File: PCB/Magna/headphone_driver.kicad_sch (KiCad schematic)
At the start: 0 parts

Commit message: Update analogue frontend and add potentiometer interface
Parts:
- added C1201, C1204: 100n, symbol Device:C
- added C1202, C1203, C1205, C1206, C1207, C1208: 100u, symbol Device:C_Polarized
- added C1209, C1210: 22uF, symbol Device:C_Polarized
- added C1211, C1212: 100pF, symbol Device:C
- added C1213, C1214: 220uF, symbol Device:C_Polarized
- added J1201: AudioJack3, symbol Connector_Audio:AudioJack3
- added R1201, R1202: 4R7, symbol Device:R
- added R1203, R1204: 10k, symbol Device:R
- added R1205, R1206, R1211, R1212: 22k, symbol Device:R
- added R1207, R1208: 680R, symbol Device:R
- added R1209, R1210: 1k3, symbol Device:R
- added R1213, R1214: 100R, symbol Device:R
- added RV1201: 10k, symbol Device:R_Potentiometer_Dual_Separate
- added U1201, U1202: NE5532, symbol Amplifier_Operational:NE5532
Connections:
- new net: C1212.2, C1214.1, R1210.2, RV1201.4, U1202.7
- new net: C1210.1, RV1201.5
- new net: C1208.2, RV1201.6
- new net: C1202.2, C1204.1, J1201.R
- new net: C1201.1, C1203.2, J1201.T
- new net: C1209.2, R1205.1, U1201.3 (+)
- new net: R1207.1, U1201.1, U1201.2 (-)
- new net: C1211.2, C1213.1, R1209.2, RV1201.1, U1201.7
- new net: C1213.2, R1211.1, R1213.1
- new net: R1208.1, U1202.1, U1202.2 (-)
- new net: C1212.1, R1208.2, R1210.1, U1202.6 (-)
- new net: C1209.1, RV1201.2
- new net: C1207.2, RV1201.3
- new net: C1214.2, R1212.1, R1214.1
- new net: R1204.1, R1214.2
- new net: R1203.1, R1213.2
- new net: C1210.2, R1206.1, U1202.3 (+)
- new net: C1211.1, R1207.2, R1209.1, U1201.6 (-)
- new net: C1204.2, R1202.1
- new net: C1201.2, R1201.1
- new net AudioInL: C1207.1
- new net AudioInR: C1208.1
- new net GND: J1201.S, R1201.2, R1202.2
- new net VAA_BIAS_L: C1205.2, R1203.2, R1205.2, R1211.2, U1201.5 (+)
- new net VAA_BIAS_R: C1206.2, R1204.2, R1206.2, R1212.2, U1202.5 (+)
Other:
- note added: "TDA2822D"

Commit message: Add final touched to all schematics
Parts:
- added C1215, C1216: 100nF/16V, Capacitor_SMD:C_0402_1005Metric, symbol Device:C
- added unit 3 of U1201
- added unit 3 of U1202
- renumbered C1207 to C1201, C1208 to C1202, C1209 to C1203, C1210 to C1204, C1211 to C1205, C1212 to C1206, C1213 to C1207, C1214 to C1208, C1205 to C1209, C1206 to C1210, C1203 to C1211, C1202 to C1212, C1201 to C1213, C1204 to C1214, R1205 to R1201, R1206 to R1202, R1207 to R1203, R1208 to R1204, R1209 to R1205, R1210 to R1206, R1211 to R1207, R1212 to R1208, R1213 to R1209, R1214 to R1210, R1203 to R1211, R1204 to R1212, R1201 to R1213, R1202 to R1214
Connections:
- net GND: now also C1215.2, C1216.2, U1201.4 (V-), U1202.4 (V-)
- new net VAA: C1215.1, C1216.1, U1201.8 (V+), U1202.8 (V+)

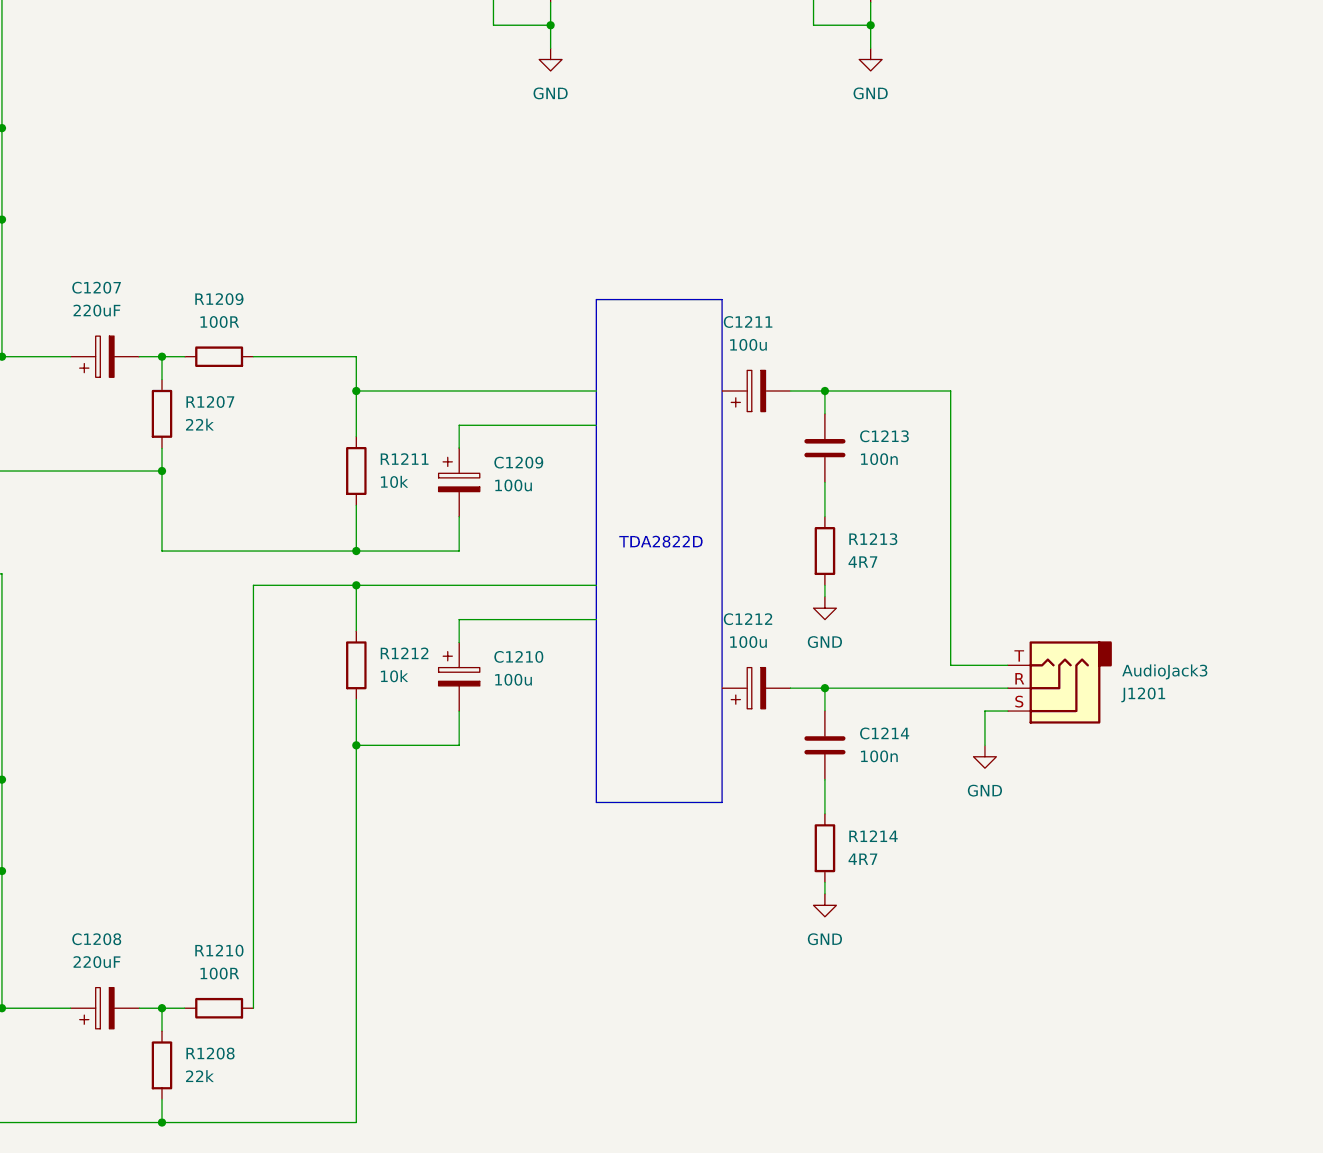
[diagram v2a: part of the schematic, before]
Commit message: Remove all ERC in schematics
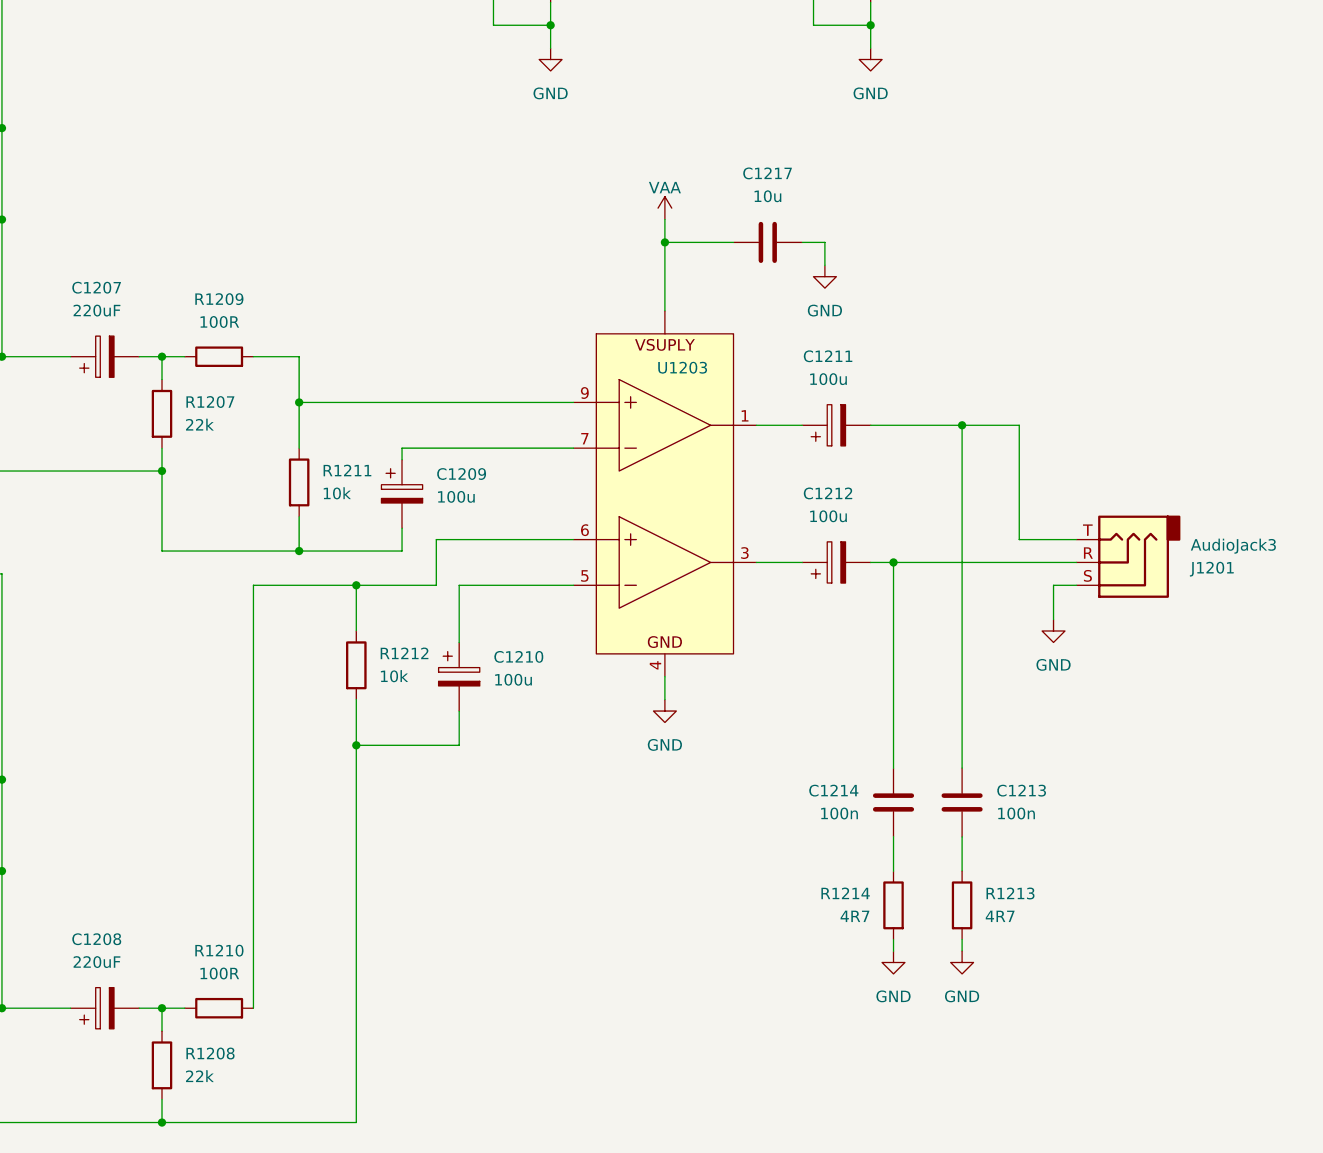
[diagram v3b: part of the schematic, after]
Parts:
- added C1217: 10u, symbol Device:C
- added U1203: ~, symbol Skrooter_symbols:TDA2822D
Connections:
- net GND: now also C1217.2, U1203.4 (GND)
- net VAA: now also C1217.1, U1203. (VCC)
- net at C1210.1: now also U1203.5 (Input2+)
- net at C1209.1: now also U1203.7 (Input1+)
- net at R1210.2, R1212.1: now also U1203.6 (Input2-)
- net at R1209.2, R1211.1: now also U1203.9 (Input1-)
- net at C1212.1: now also U1203.3 (OUTPUT2)
- net at C1211.1: now also U1203.1 (OUTPUT1)
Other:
- note removed: "TDA2822D"
- moved on the sheet: C1209, C1211, C1212, C1213, C1214, J1201, R1211, R1213, R1214

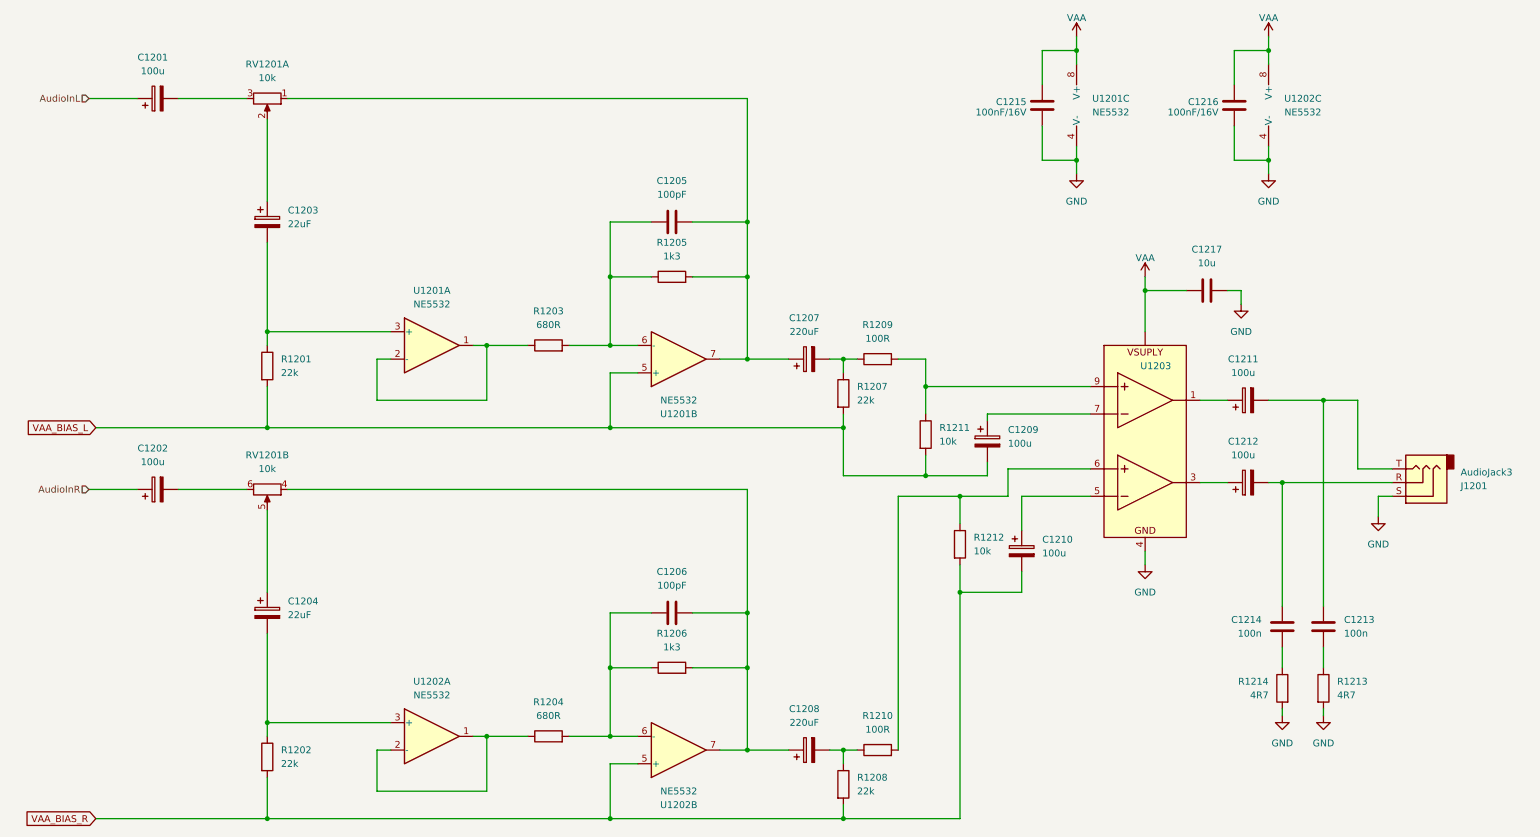
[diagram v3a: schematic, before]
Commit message: Update capacitors to parts in JLC library
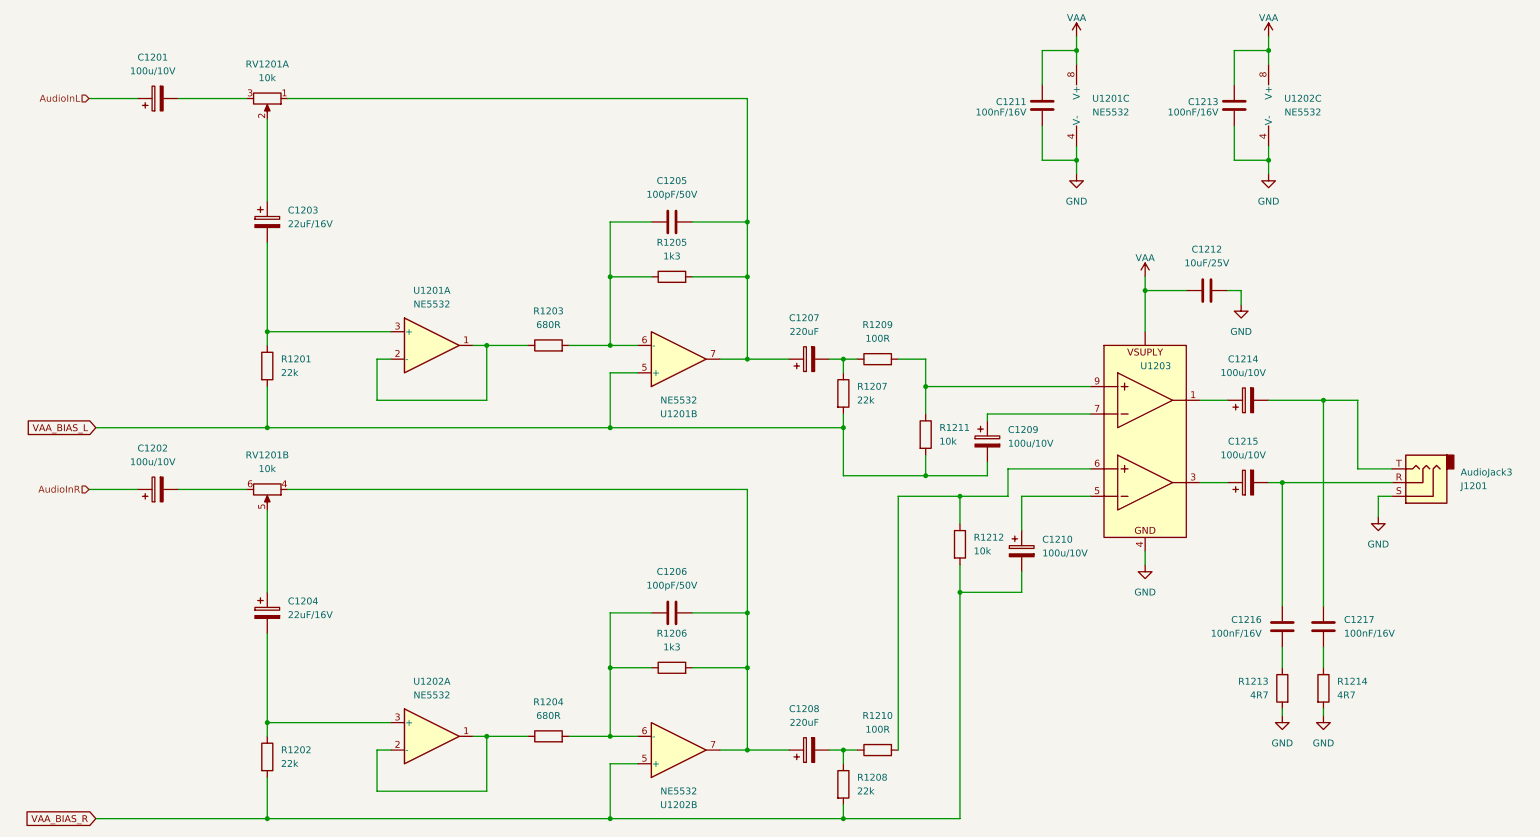
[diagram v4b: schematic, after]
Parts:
- C1201, C1202, C1209, C1210: value 100u -> 100u/10V; footprint (none) -> Capacitor_SMD:CP_Elec_6.3x5.8; LCSC (none) -> C2166157
- C1203, C1204: value 22uF -> 22uF/16V; footprint (none) -> Capacitor_SMD:CP_Elec_5x5.8; LCSC (none) -> C2163245
- C1205, C1206: value 100pF -> 100pF/50V; footprint (none) -> Capacitor_SMD:C_0805_2012Metric; LCSC (none) -> C1790
- C1207, C1208: footprint (none) -> Capacitor_SMD:CP_Elec_4x5.8; LCSC (none) -> C2165067
- C1211: renamed from C1215; footprint Capacitor_SMD:C_0402_1005Metric -> Capacitor_SMD:C_0805_2012Metric; LCSC C1525 -> C218638
- C1212: renamed from C1217; value 10u -> 10uF/25V; footprint (none) -> Capacitor_SMD:CP_Elec_4x5.8; LCSC (none) -> C2163094
- C1213: renamed from C1216; footprint Capacitor_SMD:C_0402_1005Metric -> Capacitor_SMD:C_0805_2012Metric; LCSC C1525 -> C218638
- C1214: renamed from C1211; value 100u -> 100u/10V; footprint (none) -> Capacitor_SMD:CP_Elec_6.3x5.8; LCSC (none) -> C2166157
- C1215: renamed from C1212; value 100u -> 100u/10V; footprint (none) -> Capacitor_SMD:CP_Elec_6.3x5.8; LCSC (none) -> C2166157
- C1216: renamed from C1214; value 100n -> 100nF/16V; footprint (none) -> Capacitor_SMD:C_0805_2012Metric; LCSC (none) -> C218638
- C1217: renamed from C1213; value 100n -> 100nF/16V; footprint (none) -> Capacitor_SMD:C_0805_2012Metric; LCSC (none) -> C218638
- renumbered R1214 to R1213, R1213 to R1214
